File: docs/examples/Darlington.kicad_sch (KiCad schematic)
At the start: 2 parts, among them Q1 Q_NPN, Q2 Q_NPN

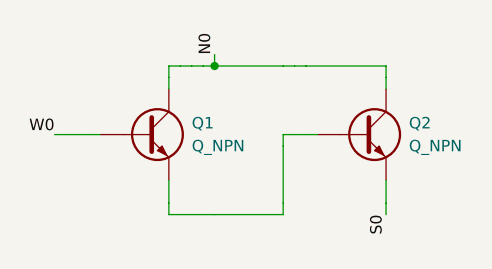
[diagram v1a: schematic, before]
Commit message: ERC-clean KiCad export: project + sym-lib-table, test points on open ports, automatic PWR_FLAGs from geometry nets; ERC (errors+warnings) asserted in tests
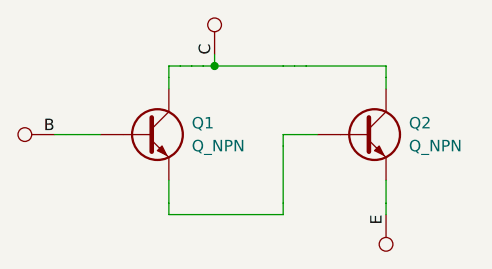
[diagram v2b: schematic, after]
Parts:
- added TP1, TP2, TP3: TestPoint, symbol Connector:TestPoint
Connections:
- net N0 renamed C
- net C: now also TP1.1
- net S0 renamed E
- net E: now also TP2.1
- net W0 renamed B
- net B: now also TP3.1
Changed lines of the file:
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@@
 		(color 0 0 0 0)
 	)
-	(label "N0"
+	(label "C"
 		(at 43.18 25.4 90)
 		(effects
@@
 		)
 	)
-	(label "S0"
+	(label "E"
 		(at 62.23 43.18 270)
 		(effects
@@
 		)
 	)
-	(label "W0"
+	(label "B"
 		(at 25.4 34.29 180)
 		(effects
@@
 		(instances
 			(project "Darlington"
-				(path "/78bfcc7e-1ac2-4ca5-b117-e940f0206eba"
+				(path "/b06c90fa-a3b3-4948-ab2c-9f3f24eb7e78"
 					(reference "Q1")
 					(unit 1)
@@
 		(instances
 			(project "Darlington"
-				(path "/78bfcc7e-1ac2-4ca5-b117-e940f0206eba"
+				(path "/b06c90fa-a3b3-4948-ab2c-9f3f24eb7e78"
 					(reference "Q2")
 					(unit 1)
 				)
+			)
+		)
+	)
+	(symbol
+		(lib_id "Connector:TestPoint")
+		(at 43.18 25.4 0)
+		(unit 1)
+		(exclude_from_sim yes)
+		(in_bom no)
+		(on_board yes)
+		(dnp no)
+		(property "Reference" "TP1"
+			(at 43.18 25.4 0)
+			(effects
+				(font
+					(size 1.27 1.27)
+				)
+				(hide yes)
+			)
+		)
+		(property "Value" "TestPoint"
+			(at 43.18 25.4 0)
+			(effects
+				(font
+					(size 1.27 1.27)
+				)
+				(hide yes)
+			)
+		)
+		(property "Footprint" ""
+			(at 43.18 25.4 0)
+			(effects
+				(font
+					(size 1.27 1.27)
+				)
+				(hide yes)
+			)
+		)
+		(property "Datasheet" ""
+			(at 43.18 25.4 0)
+			(effects
+				(font
+					(size 1.27 1.27)
+				)
+				(hide yes)
+			)
+		)
+		(pin "1"
+		)
+		(instances
+			(project "Darlington"
+				(path "/b06c90fa-a3b3-4948-ab2c-9f3f24eb7e78"
+					(reference "TP1")
+					(unit 1)
+				)
+			)
+		)
+	)
+	(symbol
+		(lib_id "Connector:TestPoint")
+		(at 62.23 43.18 180)
+		(unit 1)
+		(exclude_from_sim yes)
+		(in_bom no)
+		(on_board yes)
+		(dnp no)
+		(property "Reference" "TP2"
+			(at 62.23 43.18 0)
+			(effects
+				(font
+					(size 1.27 1.27)
+				)
+				(hide yes)
+			)
+		)
+		(property "Value" "TestPoint"
+			(at 62.23 43.18 0)
+			(effects
+				(font
+					(size 1.27 1.27)
+				)
+				(hide yes)
+			)
+		)
+		(property "Footprint" ""
+			(at 62.23 43.18 0)
+			(effects
+				(font
+					(size 1.27 1.27)
+				)
+				(hide yes)
+			)
+		)
+		(property "Datasheet" ""
+			(at 62.23 43.18 0)
+			(effects
+				(font
+					(size 1.27 1.27)
+				)
+				(hide yes)
+			)
+		)
+		(pin "1"
+		)
+		(instances
+			(project "Darlington"
+				(path "/b06c90fa-a3b3-4948-ab2c-9f3f24eb7e78"
+					(reference "TP2")
+					(unit 1)
+				)
+			)
+		)
+	)
+	(symbol
+		(lib_id "Connector:TestPoint")
+		(at 25.4 34.29 90)
+		(unit 1)
+		(exclude_from_sim yes)
+		(in_bom no)
+		(on_board yes)
+		(dnp no)
+		(property "Reference" "TP3"
+			(at 25.4 34.29 90)
+			(effects
+				(font
+					(size 1.27 1.27)
+				)
+				(hide yes)
+			)
+		)
+		(property "Value" "TestPoint"
+			(at 25.4 34.29 90)
+			(effects
+				(font
+					(size 1.27 1.27)
+				)
+				(hide yes)
+			)
+		)
+		(property "Footprint" ""
+			(at 25.4 34.29 90)
+			(effects
+				(font
+					(size 1.27 1.27)
+				)
+				(hide yes)
+			)
+		)
+		(property "Datasheet" ""
+			(at 25.4 34.29 90)
+			(effects
+				(font
+					(size 1.27 1.27)
+				)
+				(hide yes)
+			)
+		)
+		(pin "1"
+		)
+		(instances
+			(project "Darlington"
+				(path "/b06c90fa-a3b3-4948-ab2c-9f3f24eb7e78"
+					(reference "TP3")
+					(unit 1)
+				)
